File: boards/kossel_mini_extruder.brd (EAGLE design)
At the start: 66.9 x 57.9 mm, 34 parts

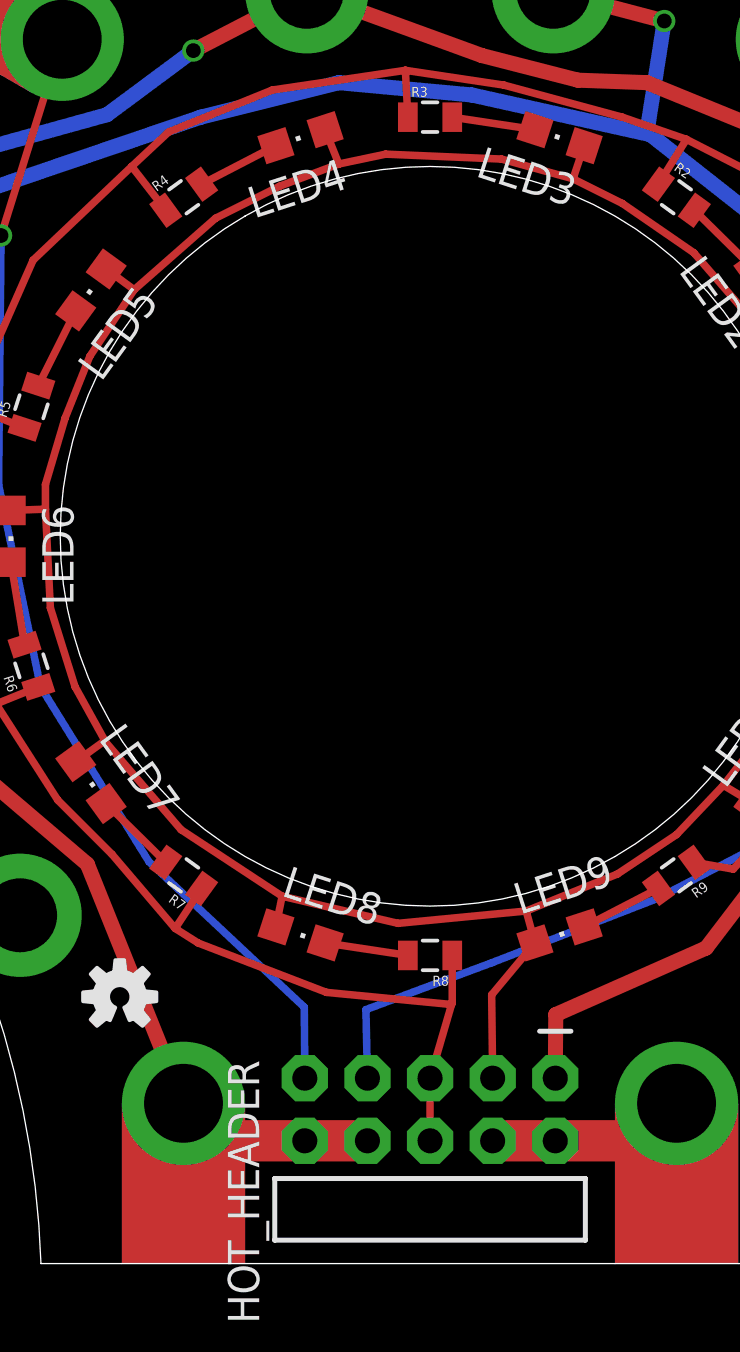
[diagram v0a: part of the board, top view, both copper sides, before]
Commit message: finished first draft of extruder and daughter boards
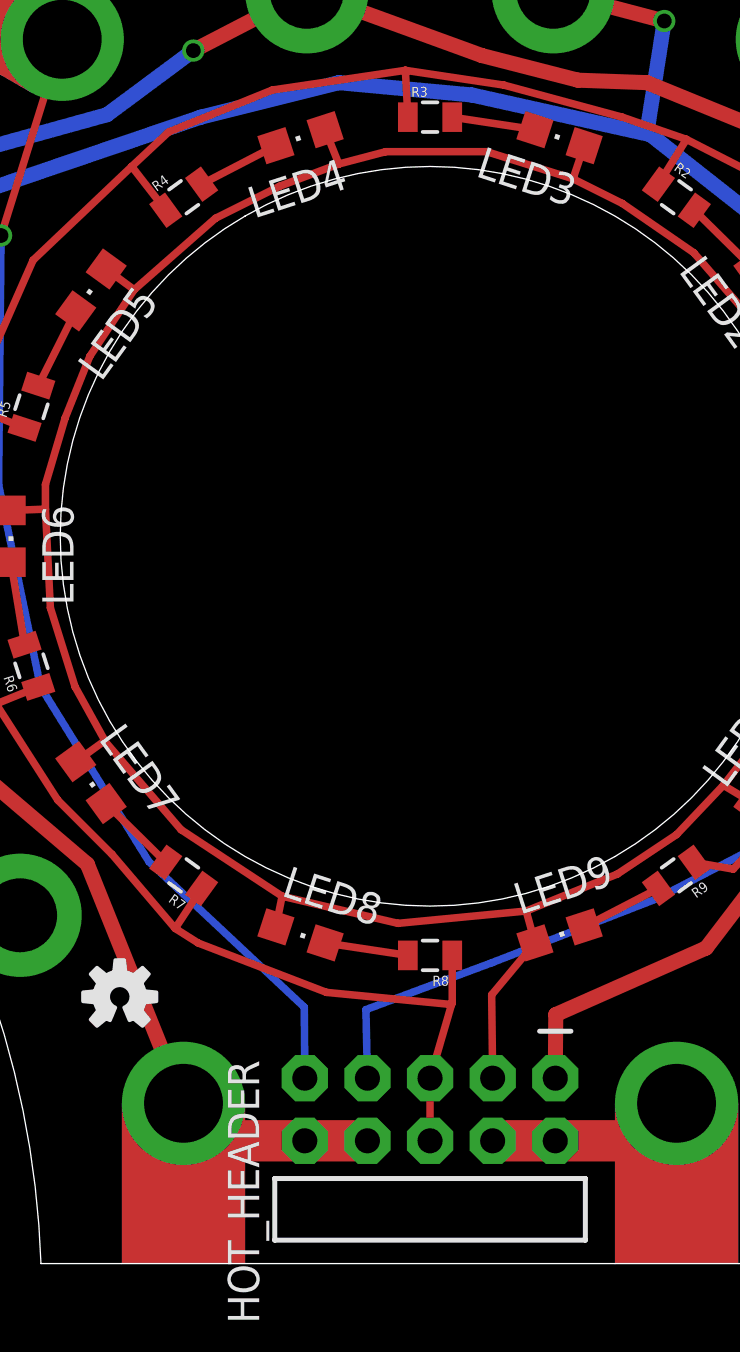
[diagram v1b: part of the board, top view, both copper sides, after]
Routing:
- net N$10: track 125.5 -> 126.4 mm
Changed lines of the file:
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@@
 <wire x1="24.3" y1="41.9" x2="21" y2="39" width="0.3048" layer="1"/>
 <wire x1="39.25189375" y1="44.843490625" x2="38.8" y2="43.5" width="0.3048" layer="1"/>
-<wire x1="38.8" y1="43.5" x2="35.9" y2="44.3" width="0.3048" layer="1"/>
-<wire x1="35.9" y1="44.3" x2="31.2" y2="44.5" width="0.3048" layer="1"/>
-<wire x1="31.2" y1="44.5" x2="29.3" y2="44.1" width="0.3048" layer="1"/>
+<wire x1="38.8" y1="43.5" x2="35.3" y2="44.6" width="0.3048" layer="1"/>
+<wire x1="35.3" y1="44.6" x2="31.2" y2="44.6" width="0.3048" layer="1"/>
+<wire x1="31.2" y1="44.6" x2="29.3" y2="44.1" width="0.3048" layer="1"/>
 <wire x1="47.370459375" y1="38.14288125" x2="46.3" y2="37.5" width="0.3048" layer="1"/>
 <wire x1="46.3" y1="37.5" x2="43.7" y2="40.5" width="0.3048" layer="1"/>
@@
 <contactref element="HOT_12V" pad="P$2"/>
 <contactref element="HOT_12V" pad="P$3"/>
-<wire x1="23" y1="6" x2="24.52" y2="4.48" width="1.6764" layer="1"/>
-<wire x1="24.52" y1="4.48" x2="27.92" y2="4.48" width="1.6764" layer="1"/>
-<wire x1="24.52" y1="4.48" x2="23" y2="2.75" width="0.2" layer="1"/>
 <contactref element="HOT_HEADER" pad="8"/>
 <wire x1="27.92" y1="4.48" x2="30.46" y2="4.48" width="1.6764" layer="1"/>
@@
 <wire x1="19.1" y1="15.7" x2="11.37383125" y2="22.287628125" width="0.6096" layer="1"/>
 <wire x1="23" y1="2.75" x2="23" y2="2.75" width="0" layer="19" extent="1-16"/>
+<wire x1="27.92" y1="4.48" x2="24.52" y2="4.48" width="1.6764" layer="1"/>
+<wire x1="24.52" y1="4.48" x2="23" y2="6" width="1.6764" layer="1"/>
+<wire x1="23" y1="6" x2="23" y2="2.75" width="1.6764" layer="1"/>
 </signal>
 <signal name="N$11">

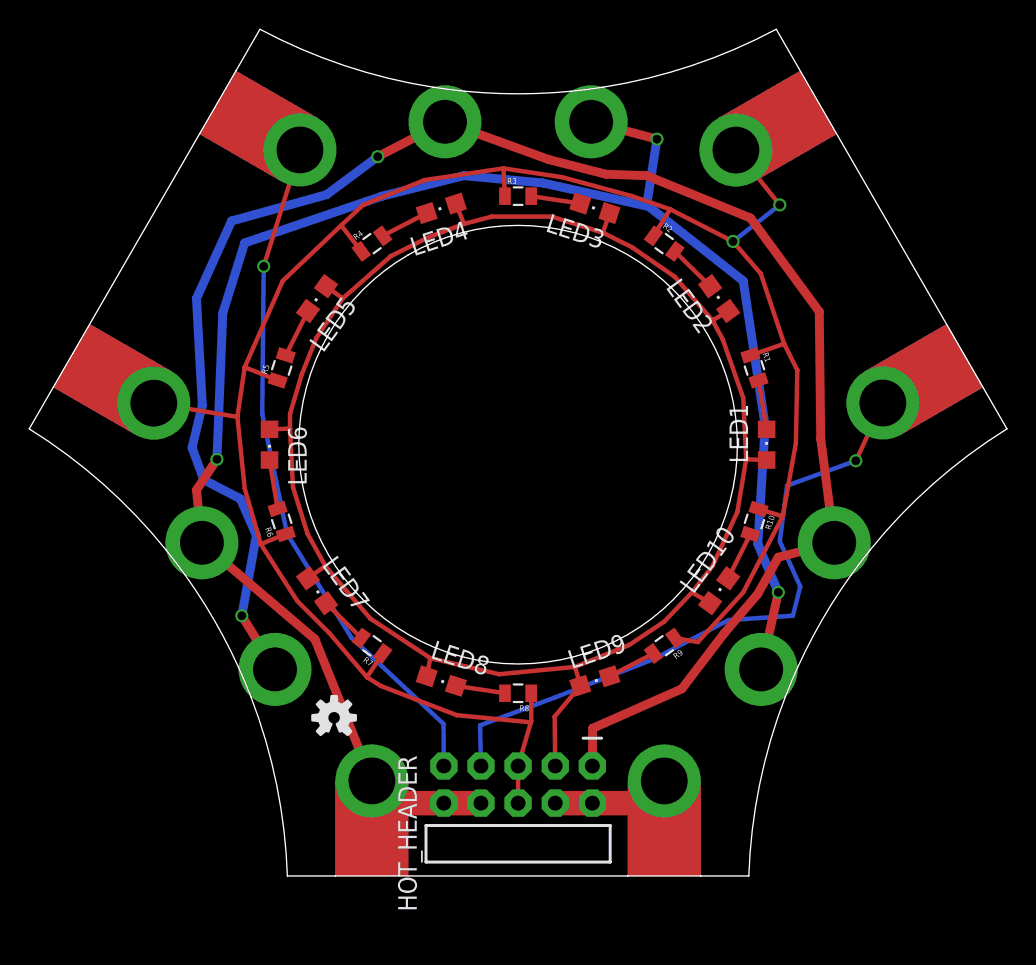
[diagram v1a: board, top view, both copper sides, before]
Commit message: made vias beefier for hand soldering
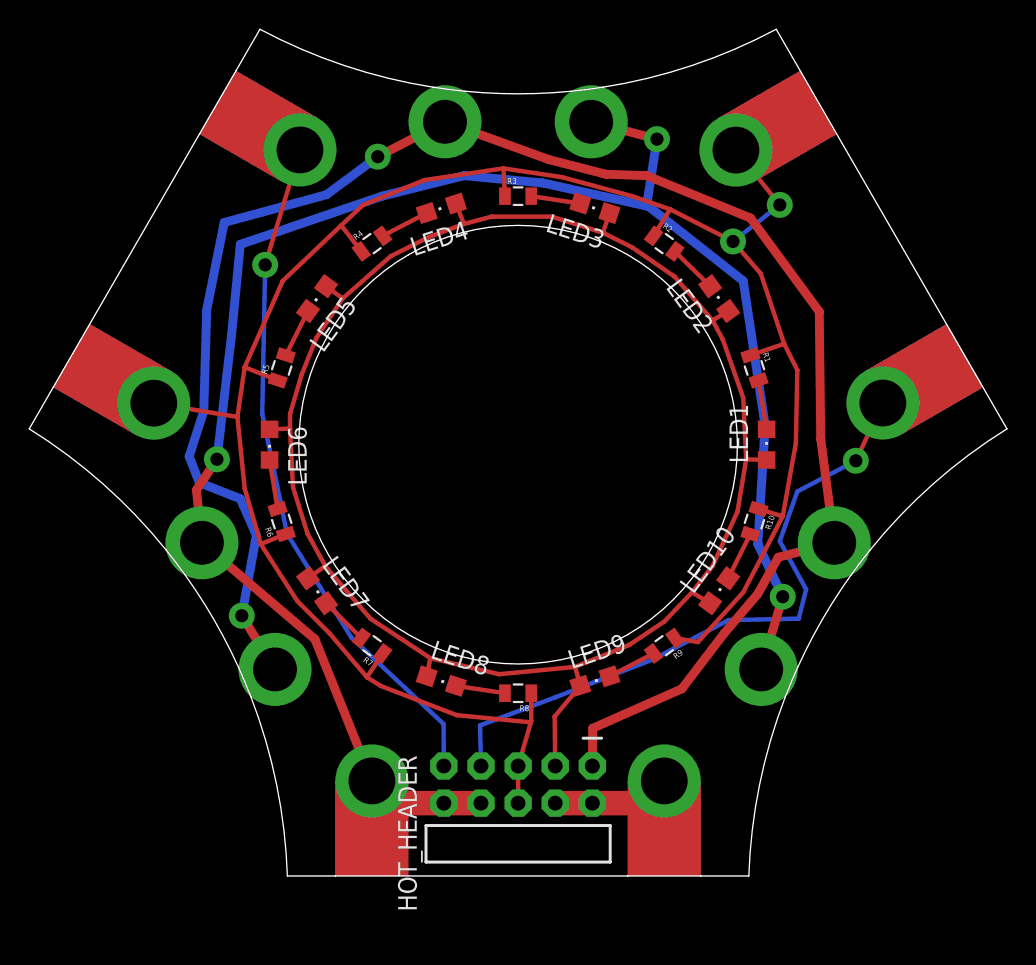
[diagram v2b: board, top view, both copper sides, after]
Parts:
- removed LOGO1: OSHW-LOGOS, SparkFun-Aesthetics:OSHW-LOGO-S
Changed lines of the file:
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@@
 <element name="FAN_1_12V" library="OBKP_Effector_PCB" package="2.3MM" value="LUG2.3" x="49.627128125" y="13.626965625" rot="R330"/>
 <element name="FAN_1_PWM" library="OBKP_Effector_PCB" package="2.3MM" value="LUG2.3" x="54.62690625" y="22.28709375" rot="R330"/>
-<element name="LOGO1" library="SparkFun-Aesthetics" package="OSHW-LOGO-S" value="OSHW-LOGOS" x="20.41443125" y="10.32013125"/>
 <element name="LED7" library="SparkFun-LED" package="CHIPLED_0805" value="" x="19.2467125" y="19.00765" rot="R306"/>
 <element name="LED8" library="SparkFun-LED" package="CHIPLED_0805" value="" x="27.7467125" y="12.832040625" rot="R342"/>
@@
 <wire x1="48.4" y1="18.9" x2="51.1" y2="24.1" width="0.3048" layer="1"/>
 <wire x1="13.8" y1="30.9" x2="8.08193125" y2="31.839365625" width="0.3048" layer="1"/>
-<via x="47.7" y="42.9" extent="1-16" drill="0.6"/>
+<via x="47.7" y="42.9" extent="1-16" drill="0.9" diameter="1.778"/>
 <wire x1="47.7" y1="42.9" x2="50.9" y2="45.4" width="0.3048" layer="16"/>
-<via x="50.9" y="45.4" extent="1-16" drill="0.6"/>
+<via x="50.9" y="45.4" extent="1-16" drill="0.9" diameter="1.778"/>
 <wire x1="50.9" y1="45.4" x2="47.9" y2="49.15" width="0.3048" layer="1"/>
 <wire x1="8.08193125" y1="31.839365625" x2="5.267346875" y2="33.464365625" width="0.6096" layer="1"/>
@@
 <contactref element="FAN_1_12V" pad="P$1"/>
 <wire x1="38.000403125" y1="51.085034375" x2="42.5" y2="49.9" width="0.6096" layer="1"/>
-<via x="42.5" y="49.9" extent="1-16" drill="0.6"/>
+<via x="42.5" y="49.9" extent="1-16" drill="0.9" diameter="1.778"/>
 <wire x1="29.3" y1="47.4" x2="23.7" y2="46" width="0.6096" layer="16"/>
-<wire x1="23.7" y1="46" x2="14.3" y2="42.8" width="0.6096" layer="16"/>
-<wire x1="14.3" y1="42.8" x2="12.8" y2="38" width="0.6096" layer="16"/>
-<wire x1="12.8" y1="38" x2="12.4" y2="28" width="0.6096" layer="16"/>
-<via x="12.4" y="28" extent="1-16" drill="0.6"/>
+<wire x1="23.7" y1="46" x2="14" y2="42.7" width="0.6096" layer="16"/>
+<wire x1="14" y1="42.7" x2="13.4" y2="36.5" width="0.6096" layer="16"/>
+<wire x1="13.4" y1="36.5" x2="12.4" y2="28" width="0.6096" layer="16"/>
+<via x="12.4" y="28" extent="1-16" drill="0.9" diameter="1.778"/>
 <wire x1="12.4" y1="28" x2="11" y2="25.9" width="0.6096" layer="1"/>
 <wire x1="11" y1="25.9" x2="11.37383125" y2="22.287628125" width="0.6096" layer="1"/>
-<wire x1="49.627128125" y1="13.626965625" x2="50.8" y2="18.9" width="0.6096" layer="1"/>
-<via x="50.8" y="18.9" extent="1-16" drill="0.6"/>
-<wire x1="50.8" y1="18.9" x2="49.4" y2="22.2" width="0.6096" layer="16"/>
+<wire x1="49.627128125" y1="13.626965625" x2="51.1" y2="18.6" width="0.6096" layer="1"/>
+<via x="51.1" y="18.6" extent="1-16" drill="0.9" diameter="1.778"/>
+<wire x1="51.1" y1="18.6" x2="49.4" y2="22.2" width="0.6096" layer="16"/>
 <wire x1="48.4" y1="40.2" x2="41.9364875" y2="45.292465625" width="0.6096" layer="16"/>
 <wire x1="41.9364875" y1="45.292465625" x2="41.8" y2="45.4" width="0.6096" layer="16"/>
@@
 <contactref element="THERM_SIG" pad="P$1"/>
 <contactref element="HOT_HEADER" pad="9"/>
-<wire x1="18.0814875" y1="49.15961875" x2="15.6" y2="41.2" width="0.3048" layer="1"/>
-<via x="15.6" y="41.2" extent="1-16" drill="0.6"/>
-<wire x1="15.6" y1="41.2" x2="15.5" y2="31.1" width="0.3048" layer="16"/>
+<wire x1="18.0814875" y1="49.15961875" x2="15.7" y2="41.3" width="0.3048" layer="1"/>
+<via x="15.7" y="41.3" extent="1-16" drill="0.9" diameter="1.778"/>
+<wire x1="15.7" y1="41.3" x2="15.5" y2="31.1" width="0.3048" layer="16"/>
 <wire x1="15.5" y1="31.1" x2="17.2" y2="22.9" width="0.3048" layer="16"/>
 <wire x1="17.2" y1="22.9" x2="21.6" y2="15.8" width="0.3048" layer="16"/>
@@
 <wire x1="35.5" y1="11.7" x2="42.2" y2="14.3" width="0.3048" layer="16"/>
 <wire x1="42.2" y1="14.3" x2="47.4" y2="17" width="0.3048" layer="16"/>
-<wire x1="47.4" y1="17" x2="51.8" y2="17.3" width="0.3048" layer="16"/>
-<wire x1="51.8" y1="17.3" x2="52.3" y2="19.3" width="0.3048" layer="16"/>
-<wire x1="52.3" y1="19.3" x2="50.9" y2="22.4" width="0.3048" layer="16"/>
-<wire x1="50.9" y1="22.4" x2="51.4" y2="26.2" width="0.3048" layer="16"/>
-<wire x1="51.4" y1="26.2" x2="56.1" y2="27.9" width="0.3048" layer="16"/>
-<via x="56.1" y="27.9" extent="1-16" drill="0.6"/>
+<wire x1="47.4" y1="17" x2="52.2" y2="17.1" width="0.3048" layer="16"/>
+<wire x1="52.2" y1="17.1" x2="52.7" y2="19.1" width="0.3048" layer="16"/>
+<wire x1="52.7" y1="19.1" x2="50.9" y2="22.4" width="0.3048" layer="16"/>
+<wire x1="50.9" y1="22.4" x2="52.1" y2="25.8" width="0.3048" layer="16"/>
+<wire x1="52.1" y1="25.8" x2="56.1" y2="27.9" width="0.3048" layer="16"/>
+<via x="56.1" y="27.9" extent="1-16" drill="0.9" diameter="1.778"/>
 <wire x1="56.1" y1="27.9" x2="57.95" y2="31.85" width="0.3048" layer="1"/>
 <wire x1="57.95" y1="31.85" x2="60.76458125" y2="33.475" width="0.6096" layer="1"/>
@@
 <wire x1="35.1" y1="48.5" x2="28.000628125" y2="51.0851625" width="0.6096" layer="1"/>
 <wire x1="16.37383125" y1="13.62736875" x2="14.1" y2="17.3" width="0.6096" layer="1"/>
-<via x="14.1" y="17.3" extent="1-16" drill="0.6"/>
+<via x="14.1" y="17.3" extent="1-16" drill="0.9" diameter="1.778"/>
 <wire x1="14.1" y1="17.3" x2="15.1" y2="22.8" width="0.6096" layer="16"/>
-<wire x1="11" y1="39" x2="13.4" y2="44.3" width="0.6096" layer="16"/>
-<wire x1="13.4" y1="44.3" x2="19.9" y2="46.1" width="0.6096" layer="16"/>
+<wire x1="11.7" y1="38.2" x2="12.9" y2="44.2" width="0.6096" layer="16"/>
+<wire x1="12.9" y1="44.2" x2="19.9" y2="46.1" width="0.6096" layer="16"/>
 <wire x1="19.9" y1="46.1" x2="23.4" y2="48.7" width="0.6096" layer="16"/>
-<via x="23.4" y="48.7" extent="1-16" drill="0.6"/>
+<via x="23.4" y="48.7" extent="1-16" drill="0.9" diameter="1.778"/>
 <wire x1="23.4" y1="48.7" x2="28.000628125" y2="51.0851625" width="0.6096" layer="1"/>
-<wire x1="11" y1="39" x2="11.4" y2="31.7" width="0.6096" layer="16"/>
-<wire x1="11.4" y1="31.7" x2="10.7" y2="28.8" width="0.6096" layer="16"/>
-<wire x1="10.7" y1="28.8" x2="11.5" y2="26.6" width="0.6096" layer="16"/>
-<wire x1="11.5" y1="26.6" x2="14" y2="25.3" width="0.6096" layer="16"/>
+<wire x1="11.7" y1="38.2" x2="11.5" y2="31.3" width="0.6096" layer="16"/>
+<wire x1="11.5" y1="31.3" x2="10.5" y2="28.2" width="0.6096" layer="16"/>
+<wire x1="10.5" y1="28.2" x2="11.2" y2="26.4" width="0.6096" layer="16"/>
+<wire x1="11.2" y1="26.4" x2="14" y2="25.3" width="0.6096" layer="16"/>
 <wire x1="14" y1="25.3" x2="15.1" y2="22.8" width="0.6096" layer="16"/>
 <wire x1="44.2" y1="12.3" x2="47.1" y2="16.1" width="0.6096" layer="1"/>
@@
 </signal>
 </signals>
+<errors>
+</errors>
 </board>
 </drawing>
